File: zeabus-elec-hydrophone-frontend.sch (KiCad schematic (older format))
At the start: 4 parts, among them J1 Conn_R1, J2 Conn_L1, J3 Conn_R2, J4 Conn_L2

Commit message: Bug fixed 1
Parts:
- removed J1: Conn_R1, symbol Conn_01x08
- added J1: Conn_R1, symbol Conn_01x10
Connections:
- net SCL: now also J1.1 (Pin_1); no longer J4.6 (Pin_6)
- net SDA: now also J1.2 (Pin_2); no longer J4.5 (Pin_5)
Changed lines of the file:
@@
-$EndComp
-$Comp
-L Conn_01x08 J1
-U 1 1 5AD92CAB
-P 3150 4300
-F 0 "J1" H 3150 4700 50  0000 C CNN
-F 1 "Conn_R1" H 3150 3800 50  0000 C CNN
-F 2 "" H 3150 4300 50  0001 C CNN
-F 3 "" H 3150 4300 50  0001 C CNN
-	1    3150 4300
-	-1   0    0    -1
 $EndComp
 $Comp
@@
 Text Label 1600 5500 0    60   ~ 0
 ADC3
-Text Label 1600 5600 0    60   ~ 0
+Text Label 3600 3900 2    60   ~ 0
 SDA
-Text Label 1600 5700 0    60   ~ 0
+Text Label 3600 3800 2    60   ~ 0
 SCL
 Wire Wire Line
@@
 Wire Wire Line
 	1900 5500 1600 5500
-Wire Wire Line
-	1600 5600 1900 5600
-Wire Wire Line
-	1900 5700 1600 5700
 $Comp
 L GNDA #PWR3
@@
 Wire Wire Line
 	6500 3500 5950 3500
+$Comp
+L Conn_01x10 J1
+U 1 1 5AD972E3
+P 3150 4200
+F 0 "J1" H 3150 4700 50  0000 C CNN
+F 1 "Conn_R1" H 3150 3600 50  0000 C CNN
+F 2 "" H 3150 4200 50  0001 C CNN
+F 3 "" H 3150 4200 50  0001 C CNN
+	1    3150 4200
+	-1   0    0    -1
+$EndComp
+Wire Wire Line
+	3350 3800 3600 3800
+Wire Wire Line
+	3600 3900 3350 3900
 $EndSCHEMATC

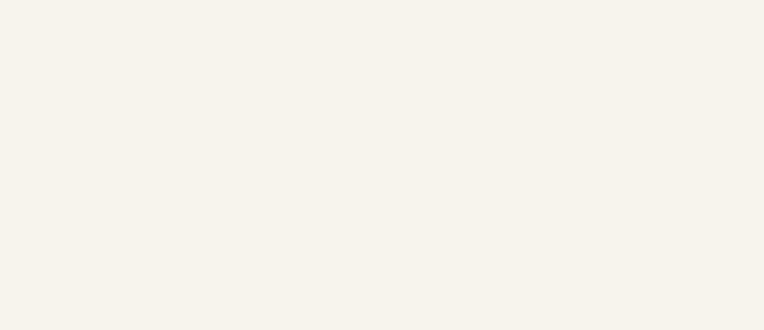
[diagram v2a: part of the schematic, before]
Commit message: Assigned footprint for dimension checking
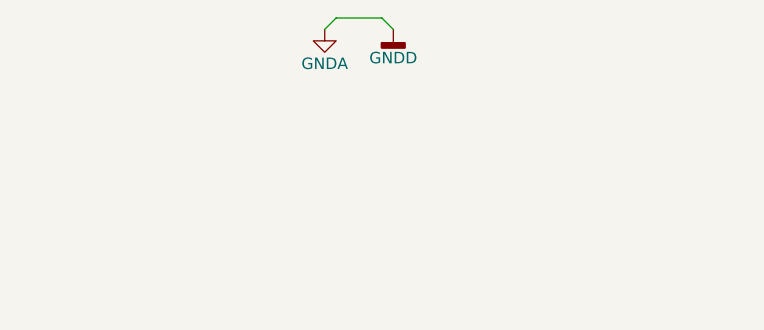
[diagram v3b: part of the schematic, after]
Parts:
- J1: footprint (none) -> Pin_Headers:Pin_Header_Straight_1x10_Pitch2.54mm
- J2, J3: footprint (none) -> Pin_Headers:Pin_Header_Straight_1x08_Pitch2.54mm
- J4: footprint (none) -> Pin_Headers:Pin_Header_Straight_1x06_Pitch2.54mm
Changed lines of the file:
@@
 LIBS:contrib
 LIBS:valves
+LIBS:zeabus
 LIBS:ftdi
 LIBS:zeabus-elec-hydrophone-frontend-cache
@@
 F 0 "J2" H 2100 4900 50  0000 C CNN
 F 1 "Conn_L1" H 2100 4000 50  0000 C CNN
-F 2 "" H 2100 4500 50  0001 C CNN
+F 2 "Pin_Headers:Pin_Header_Straight_1x08_Pitch2.54mm" H 2100 4500 50  0001 C CNN
 F 3 "" H 2100 4500 50  0001 C CNN
 	1    2100 4500
@@
 F 0 "J3" H 3150 5700 50  0000 C CNN
 F 1 "Conn_R2" H 3150 4800 50  0000 C CNN
-F 2 "" H 3150 5300 50  0001 C CNN
+F 2 "Pin_Headers:Pin_Header_Straight_1x08_Pitch2.54mm" H 3150 5300 50  0001 C CNN
 F 3 "" H 3150 5300 50  0001 C CNN
 	1    3150 5300
@@
 F 0 "J4" H 2100 5700 50  0000 C CNN
 F 1 "Conn_L2" H 2100 5000 50  0000 C CNN
-F 2 "" H 2100 5400 50  0001 C CNN
+F 2 "Pin_Headers:Pin_Header_Straight_1x06_Pitch2.54mm" H 2100 5400 50  0001 C CNN
 F 3 "" H 2100 5400 50  0001 C CNN
 	1    2100 5400
@@
 	1900 5500 1600 5500
 $Comp
-L GNDA #PWR3
+L GNDA #PWR01
 U 1 1 5AD94E9E
 P 1800 4800
-F 0 "#PWR3" H 1800 4550 50  0001 C CNN
+F 0 "#PWR01" H 1800 4550 50  0001 C CNN
 F 1 "GNDA" H 1800 4650 50  0000 C CNN
 F 2 "" H 1800 4800 50  0001 C CNN
@@
 Connection ~ 1850 4800
 $Comp
-L +5V #PWR2
+L +5V #PWR02
 U 1 1 5AD957E3
 P 1800 4600
-F 0 "#PWR2" H 1800 4450 50  0001 C CNN
+F 0 "#PWR02" H 1800 4450 50  0001 C CNN
 F 1 "+5V" H 1800 4740 50  0000 C CNN
 F 2 "" H 1800 4600 50  0001 C CNN
@@
 	1900 4600 1800 4600
 $Comp
-L +3.3V #PWR1
+L +3.3V #PWR03
 U 1 1 5AD95EFA
 P 1650 4500
-F 0 "#PWR1" H 1650 4350 50  0001 C CNN
+F 0 "#PWR03" H 1650 4350 50  0001 C CNN
 F 1 "+3.3V" H 1650 4640 50  0000 C CNN
 F 2 "" H 1650 4500 50  0001 C CNN
@@
 F 0 "J1" H 3150 4700 50  0000 C CNN
 F 1 "Conn_R1" H 3150 3600 50  0000 C CNN
-F 2 "" H 3150 4200 50  0001 C CNN
+F 2 "Pin_Headers:Pin_Header_Straight_1x10_Pitch2.54mm" H 3150 4200 50  0001 C CNN
 F 3 "" H 3150 4200 50  0001 C CNN
 	1    3150 4200
@@
 Wire Wire Line
 	3600 3900 3350 3900
+$Comp
+L GNDA #PWR04
+U 1 1 5ADC913F
+P 2800 1950
+F 0 "#PWR04" H 2800 1700 50  0001 C CNN
+F 1 "GNDA" H 2800 1800 50  0000 C CNN
+F 2 "" H 2800 1950 50  0001 C CNN
+F 3 "" H 2800 1950 50  0001 C CNN
+	1    2800 1950
+	1    0    0    -1
+$EndComp
+$Comp
+L GNDD #PWR05
+U 1 1 5ADC957D
+P 3100 1950
+F 0 "#PWR05" H 3100 1700 50  0001 C CNN
+F 1 "GNDD" H 3100 1825 50  0000 C CNN
+F 2 "" H 3100 1950 50  0001 C CNN
+F 3 "" H 3100 1950 50  0001 C CNN
+	1    3100 1950
+	1    0    0    -1
+$EndComp
+Wire Wire Line
+	2800 1950 2850 1900
+Wire Wire Line
+	2850 1900 3050 1900
+Wire Wire Line
+	3050 1900 3100 1950
 $EndSCHEMATC
